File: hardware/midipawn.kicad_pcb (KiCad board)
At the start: 2 copper layers, 124.5 x 86.4 mm, 82 parts, among them J1 MIDI I/O, J10 LOOP 8, J11 LOOP 9, J12 LOOP 10, J13 Barrel_Jack_Switch, J2 I/O, J3 LOOP 1, J4 LOOP 2, J5 LOOP 3, J6 LOOP 4, J7 LOOP 5, J8 LOOP 6, J9 LOOP 7, K1 G6S-2, K10 G6S-2, K2 G6S-2, K3 G6S-2, K4 G6S-2, K5 G6S-2, K6 G6S-2, K7 G6S-2, K8 G6S-2, K9 G6S-2, Q1 2N3904, Q10 2N3904, Q2 2N3904, Q3 2N3904, Q4 2N3904, Q5 2N3904, Q6 2N3904, Q7 2N3904, Q8 2N3904, Q9 2N3904, U1 L7805, U2 6N137

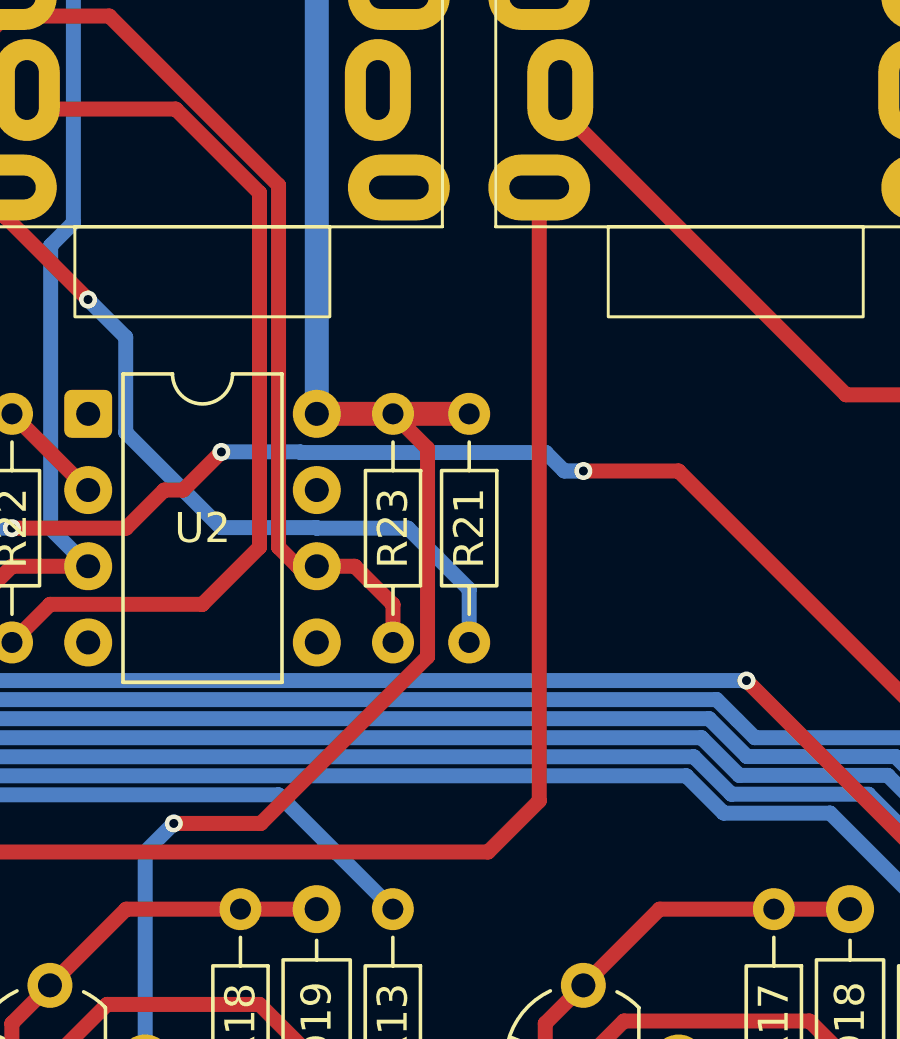
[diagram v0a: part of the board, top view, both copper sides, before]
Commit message: Add pull-down resistor on voltage regulator enable pin
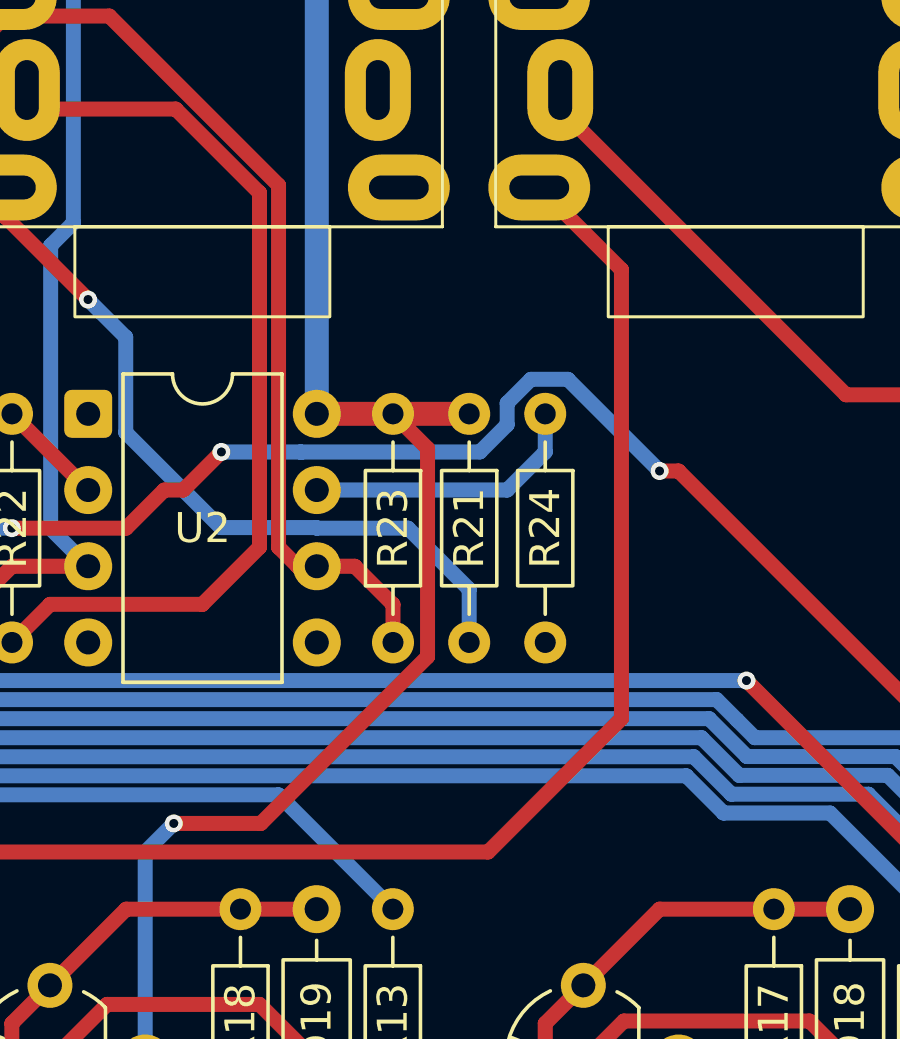
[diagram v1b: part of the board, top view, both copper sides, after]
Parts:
- added R24: 10K, Resistor_THT:R_Axial_DIN0204_L3.6mm_D1.6mm_P7.62mm_Horizontal, F.Cu at (135.9, 85.7)
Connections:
- U2 pad 7: unconnected-(U2-EN-Pad7) -> Net-(U2-EN)
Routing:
- net Net-(U2-EN): track 0.00 -> 9.41 mm
- net MCU_LOOP1: track 60.7 -> 63.1 mm
- net OUT: track 75.7 -> 77.9 mm
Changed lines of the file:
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@@
 	(net 84 "unconnected-(U2-NC-Pad4)")
 	(net 85 "unconnected-(U2-NC-Pad1)")
-	(net 86 "unconnected-(U2-EN-Pad7)")
+	(net 86 "Net-(U2-EN)")
 	(net 87 "unconnected-(RZ1-3V3-Pad21)")
 	(net 88 "unconnected-(J13-Pad3)")
@@
 		)
 	)
+	(footprint "Resistor_THT:R_Axial_DIN0204_L3.6mm_D1.6mm_P7.62mm_Horizontal"
+		(layer "F.Cu")
+		(at 135.89 85.725 -90)
+		(descr "Resistor, Axial_DIN0204 series, Axial, Horizontal, pin pitch=7.62mm, 0.167W, length*diameter=3.6*1.6mm^2, http://cdn-reichelt.de/documents/datenblatt/B400/1_4W%23YAG.pdf")
+		(tags "Resistor Axial_DIN0204 series Axial Horizontal pin pitch 7.62mm 0.167W length 3.6mm diameter 1.6mm")
+		(property "Reference" "R24"
+			(at 3.81 0 90)
+			(layer "F.SilkS")
+			(effects
+				(font
+					(size 1 1)
+					(thickness 0.15)
+				)
+			)
+		)
+		(property "Value" "10K"
+			(at 3.81 1.92 90)
+			(layer "F.Fab")
+			(effects
+				(font
+					(size 1 1)
+					(thickness 0.15)
+				)
+			)
+		)
+		(property "Datasheet" "~"
+			(at 0 0 90)
+			(layer "F.Fab")
+			(hide yes)
+			(effects
+				(font
+					(size 1.27 1.27)
+					(thickness 0.15)
+				)
+			)
+		)
+		(property "Description" "Resistor"
+			(at 0 0 90)
+			(layer "F.Fab")
+			(hide yes)
+			(effects
+				(font
+					(size 1.27 1.27)
+					(thickness 0.15)
+				)
+			)
+		)
+		(property ki_fp_filters "R_*")
+		(sheetname "/")
+		(sheetfile "midipawn.kicad_sch")
+		(attr through_hole)
+		(fp_line
+			(start 0.94 0)
+			(end 1.89 0)
+			(stroke
+				(width 0.12)
+				(type solid)
+			)
+			(layer "F.SilkS")
+		)
+		(fp_line
+			(start 6.68 0)
+			(end 5.73 0)
+			(stroke
+				(width 0.12)
+				(type solid)
+			)
+			(layer "F.SilkS")
+		)
+		(fp_rect
+			(start 1.89 -0.92)
+			(end 5.73 0.92)
+			(stroke
+				(width 0.12)
+				(type solid)
+			)
+			(fill no)
+			(layer "F.SilkS")
+		)
+		(fp_rect
+			(start -0.95 -1.05)
+			(end 8.57 1.05)
+			(stroke
+				(width 0.05)
+				(type solid)
+			)
+			(fill no)
+			(layer "F.CrtYd")
+		)
+		(fp_line
+			(start 0 0)
+			(end 2.01 0)
+			(stroke
+				(width 0.1)
+				(type solid)
+			)
+			(layer "F.Fab")
+		)
+		(fp_line
+			(start 7.62 0)
+			(end 5.61 0)
+			(stroke
+				(width 0.1)
+				(type solid)
+			)
+			(layer "F.Fab")
+		)
+		(fp_rect
+			(start 2.01 -0.8)
+			(end 5.61 0.8)
+			(stroke
+				(width 0.1)
+				(type solid)
+			)
+			(fill no)
+			(layer "F.Fab")
+		)
+		(fp_text user "${REFERENCE}"
+			(at 3.81 0 90)
+			(layer "F.Fab")
+			(effects
+				(font
+					(size 0.72 0.72)
+					(thickness 0.108)
+				)
+			)
+		)
+		(pad "1" thru_hole circle
+			(at 0 0 270)
+			(size 1.4 1.4)
+			(drill 0.7)
+			(layers "*.Cu" "*.Mask")
+			(remove_unused_layers no)
+			(net 86 "Net-(U2-EN)")
+			(pintype "passive")
+		)
+		(pad "2" thru_hole circle
+			(at 7.62 0 270)
+			(size 1.4 1.4)
+			(drill 0.7)
+			(layers "*.Cu" "*.Mask")
+			(remove_unused_layers no)
+			(net 1 "GND")
+			(pintype "passive")
+		)
+		(embedded_fonts no)
+		(model "${KICAD9_3DMODEL_DIR}/Resistor_THT.3dshapes/R_Axial_DIN0204_L3.6mm_D1.6mm_P7.62mm_Horizontal.step"
+			(offset
+				(xyz 0 0 0)
+			)
+			(scale
+				(xyz 1 1 1)
+			)
+			(rotate
+				(xyz 0 0 0)
+			)
+		)
+	)
 	(footprint "midipawn:CK635-037"
 		(layer "F.Cu")
@@
 			(layers "*.Cu" "*.Mask")
 			(remove_unused_layers no)
-			(net 86 "unconnected-(U2-EN-Pad7)")
+			(net 86 "Net-(U2-EN)")
 			(pinfunction "EN")
 			(pintype "input")
@@
 	)
 	(segment
-		(start 96.066 111.579)
-		(end 97.155 110.49)
+		(start 90.17 113.03)
+		(end 91.621 111.579)
 		(width 0.5)
 		(layer "F.Cu")
@@
 	)
 	(segment
-		(start 100.965 100.33)
-		(end 133.985 100.33)
+		(start 97.155 104.14)
+		(end 100.965 100.33)
 		(width 0.5)
 		(layer "F.Cu")
@@
 	)
 	(segment
-		(start 90.17 113.03)
-		(end 91.621 111.579)
+		(start 97.155 110.49)
+		(end 97.155 104.14)
 		(width 0.5)
 		(layer "F.Cu")
@@
 	)
 	(segment
-		(start 97.155 110.49)
-		(end 97.155 104.14)
+		(start 133.985 100.33)
+		(end 138.43 95.885)
 		(width 0.5)
 		(layer "F.Cu")
@@
 	)
 	(segment
-		(start 97.155 104.14)
-		(end 100.965 100.33)
+		(start 138.43 80.92)
+		(end 135.69 78.18)
 		(width 0.5)
 		(layer "F.Cu")
@@
 	)
 	(segment
-		(start 133.985 100.33)
-		(end 135.69 98.625)
+		(start 96.066 111.579)
+		(end 97.155 110.49)
 		(width 0.5)
 		(layer "F.Cu")
@@
 	)
 	(segment
-		(start 135.69 98.625)
-		(end 135.69 78.18)
+		(start 138.43 95.885)
+		(end 138.43 80.92)
+		(width 0.5)
+		(layer "F.Cu")
+		(net 34)
+	)
+	(segment
+		(start 100.965 100.33)
+		(end 133.985 100.33)
 		(width 0.5)
 		(layer "F.Cu")
@@
 	)
 	(segment
+		(start 140.335 87.63)
+		(end 139.7 87.63)
+		(width 0.5)
+		(layer "F.Cu")
+		(net 74)
+	)
+	(segment
 		(start 123.825 88.265)
 		(end 123.19 88.265)
@@
 	)
 	(segment
-		(start 140.335 87.63)
-		(end 137.16 87.63)
+		(start 153.67 100.965)
+		(end 140.335 87.63)
 		(width 0.5)
 		(layer "F.Cu")
@@
 	)
 	(segment
-		(start 153.67 100.965)
-		(end 140.335 87.63)
-		(width 0.5)
-		(layer "F.Cu")
-		(net 74)
-	)
-	(segment
 		(start 125.095 86.995)
 		(end 123.825 88.265)
@@
 	)
 	(via
-		(at 137.16 87.63)
+		(at 139.7 87.63)
 		(size 0.6)
 		(drill 0.3)
@@
 	)
 	(segment
+		(start 133.71276 86.995)
+		(end 134.62 86.08776)
+		(width 0.5)
+		(layer "B.Cu")
+		(net 74)
+	)
+	(segment
+		(start 135.41324 84.574)
+		(end 136.644 84.574)
+		(width 0.5)
+		(layer "B.Cu")
+		(net 74)
+	)
+	(segment
 		(start 104.14 83.185)
 		(end 109.855 88.9)
@@
 	)
 	(segment
-		(start 110.49 89.535)
-		(end 118.11 89.535)
+		(start 136.644 84.574)
+		(end 139.7 87.63)
 		(width 0.5)
 		(layer "B.Cu")
@@
 	)
 	(segment
-		(start 137.16 87.63)
-		(end 136.525 87.63)
+		(start 110.49 89.535)
+		(end 118.11 89.535)
 		(width 0.5)
 		(layer "B.Cu")
@@
 	(segment
 		(start 127.737818 86.995)
-		(end 127.756818 87.014)
+		(end 125.095 86.995)
 		(width 0.5)
 		(layer "B.Cu")
@@
 	)
 	(segment
-		(start 136.525 87.63)
-		(end 135.909 87.014)
+		(start 127.756818 87.014)
+		(end 127.737818 86.995)
 		(width 0.5)
 		(layer "B.Cu")
@@
 	)
 	(segment
-		(start 125.095 86.995)
-		(end 127.737818 86.995)
+		(start 134.62 86.08776)
+		(end 134.62 85.36724)
 		(width 0.5)
 		(layer "B.Cu")
@@
 	)
 	(segment
-		(start 135.909 87.014)
-		(end 127.756818 87.014)
+		(start 134.62 85.36724)
+		(end 135.41324 84.574)
+		(width 0.5)
+		(layer "B.Cu")
+		(net 74)
+	)
+	(segment
+		(start 127.737818 86.995)
+		(end 133.71276 86.995)
 		(width 0.5)
 		(layer "B.Cu")
@@
 		(net 83)
 	)
+	(segment
+		(start 128.275 88.265)
+		(end 134.62 88.265)
+		(width 0.5)
+		(layer "B.Cu")
+		(net 86)
+	)
+	(segment
+		(start 135.89 86.995)
+		(end 135.89 85.725)
+		(width 0.5)
+		(layer "B.Cu")
+		(net 86)
+	)
+	(segment
+		(start 134.62 88.265)
+		(end 135.89 86.995)
+		(width 0.5)
+		(layer "B.Cu")
+		(net 86)
+	)
 	(zone
